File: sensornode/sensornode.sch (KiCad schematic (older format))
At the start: 24 parts, among them J1 Conn_01x02, J2 Conn_01x06_Male, J3 Conn_01x04_Male, J4 USB_B_Micro, Q1 MMBT3904, U1 ESP-12F, U2 MQ-135, U3 LTC4055, U4 MIC5504-3.3YM5

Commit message: update to latest
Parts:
- RV1: footprint Potentiometer_THT:Potentiometer_ACP_CA6-H2,5_Horizontal -> Potentiometer_THT:Potentiometer_Bourns_3266X_Horizontal
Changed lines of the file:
@@
 F 0 "RV1" V 7035 1550 50  0000 C CNN
 F 1 "100k" V 6944 1550 50  0000 C CNN
-F 2 "Potentiometer_THT:Potentiometer_ACP_CA6-H2,5_Horizontal" H 7150 1550 50  0001 C CNN
+F 2 "Potentiometer_THT:Potentiometer_Bourns_3266X_Horizontal" H 7150 1550 50  0001 C CNN
 F 3 "~" H 7150 1550 50  0001 C CNN
 	1    7150 1550

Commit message: add c6, relayout
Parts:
- added C6: 10u ceramic, Capacitor_SMD:C_0805_2012Metric, symbol Device:C
- added R10: 1k8, Resistor_SMD:R_0603_1608Metric, symbol Device:R
- U2: symbol Sensor_Gas:MQ-135 -> sensornode-rescue:MQ-135-Sensor_Gas
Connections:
- wire segments 101 -> 105
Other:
- moved on the sheet: RV1
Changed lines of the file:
@@
 $EndDescr
 $Comp
-L Sensor_Gas:MQ-135 U2
+L sensornode-rescue:MQ-135-Sensor_Gas U2
 U 1 1 5CC7BF70
 P 6100 1750
@@
 $EndComp
 Wire Wire Line
-	5550 1450 5150 1450
-Wire Wire Line
-	6600 1550 6750 1550
+	5550 1450 5300 1450
 Wire Wire Line
 	6600 2000 7000 2000
@@
 L power:GND #PWR016
 U 1 1 5CCBD0AA
-P 7550 1600
-F 0 "#PWR016" H 7550 1350 50  0001 C CNN
-F 1 "GND" H 7555 1427 50  0000 C CNN
-F 2 "" H 7550 1600 50  0001 C CNN
-F 3 "" H 7550 1600 50  0001 C CNN
-	1    7550 1600
+P 7750 1600
+F 0 "#PWR016" H 7750 1350 50  0001 C CNN
+F 1 "GND" H 7755 1427 50  0000 C CNN
+F 2 "" H 7750 1600 50  0001 C CNN
+F 3 "" H 7750 1600 50  0001 C CNN
+	1    7750 1600
 	1    0    0    -1
 $EndComp
@@
 L Device:R_POT RV1
 U 1 1 5CCBD83F
-P 7150 1550
-F 0 "RV1" V 7035 1550 50  0000 C CNN
-F 1 "100k" V 6944 1550 50  0000 C CNN
-F 2 "Potentiometer_THT:Potentiometer_Bourns_3266X_Horizontal" H 7150 1550 50  0001 C CNN
-F 3 "~" H 7150 1550 50  0001 C CNN
-	1    7150 1550
+P 7350 1550
+F 0 "RV1" V 7235 1550 50  0000 C CNN
+F 1 "100k" V 7144 1550 50  0000 C CNN
+F 2 "Potentiometer_THT:Potentiometer_Bourns_3266X_Horizontal" H 7350 1550 50  0001 C CNN
+F 3 "~" H 7350 1550 50  0001 C CNN
+	1    7350 1550
 	0    -1   -1   0
 $EndComp
 Wire Wire Line
-	7300 1550 7550 1550
-Wire Wire Line
-	7550 1550 7550 1600
-Wire Wire Line
-	7150 1400 7550 1400
-Wire Wire Line
-	7550 1400 7550 1550
-Connection ~ 7550 1550
-Wire Wire Line
-	6750 1550 6750 1150
-Connection ~ 6750 1550
-Wire Wire Line
-	6750 1550 7000 1550
-Text Label 6750 1300 0    50   ~ 0
+	7500 1550 7750 1550
+Wire Wire Line
+	7750 1550 7750 1600
+Wire Wire Line
+	7350 1400 7750 1400
+Wire Wire Line
+	7750 1400 7750 1550
+Connection ~ 7750 1550
+Text Label 7100 1300 0    50   ~ 0
 mq135_adc
 Wire Wire Line
@@
 Connection ~ 6150 4800
 Wire Wire Line
-	5150 2000 5550 2000
+	5150 2000 5300 2000
 $Comp
 L Connector:USB_B_Micro J4
@@
 	1    0    0    -1
 $EndComp
+$Comp
+L Device:C C6
+U 1 1 5CE46D1C
+P 5300 1850
+F 0 "C6" H 5415 1896 50  0000 L CNN
+F 1 "10u ceramic" H 5415 1805 50  0000 L CNN
+F 2 "Capacitor_SMD:C_0805_2012Metric" H 5338 1700 50  0001 C CNN
+F 3 "https://www.samsungsem.com/kr/support/product-search/mlcc/__icsFiles/afieldfile/2019/05/10/19-CL21A106KPFNNNE.pdf" H 5300 1850 50  0001 C CNN
+	1    5300 1850
+	1    0    0    -1
+$EndComp
+Connection ~ 5300 2000
+Wire Wire Line
+	5300 2000 5550 2000
+Wire Wire Line
+	5300 1700 5300 1450
+Connection ~ 5300 1450
+Wire Wire Line
+	5300 1450 5150 1450
+$Comp
+L Device:R R10
+U 1 1 5CE5CB49
+P 6850 1550
+F 0 "R10" V 6643 1550 50  0000 C CNN
+F 1 "1k8" V 6734 1550 50  0000 C CNN
+F 2 "Resistor_SMD:R_0603_1608Metric" V 6780 1550 50  0001 C CNN
+F 3 "~" H 6850 1550 50  0001 C CNN
+	1    6850 1550
+	0    1    1    0
+$EndComp
+Wire Wire Line
+	6600 1550 6700 1550
+Wire Wire Line
+	7000 1550 7100 1550
+Wire Wire Line
+	7100 1300 7100 1550
+Connection ~ 7100 1550
+Wire Wire Line
+	7100 1550 7200 1550
 $EndSCHEMATC

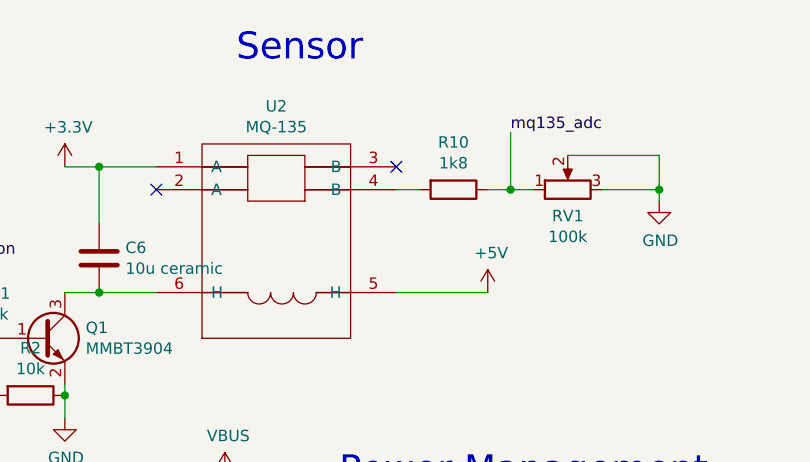
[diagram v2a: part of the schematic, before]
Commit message: tweaks, add jumper for programming
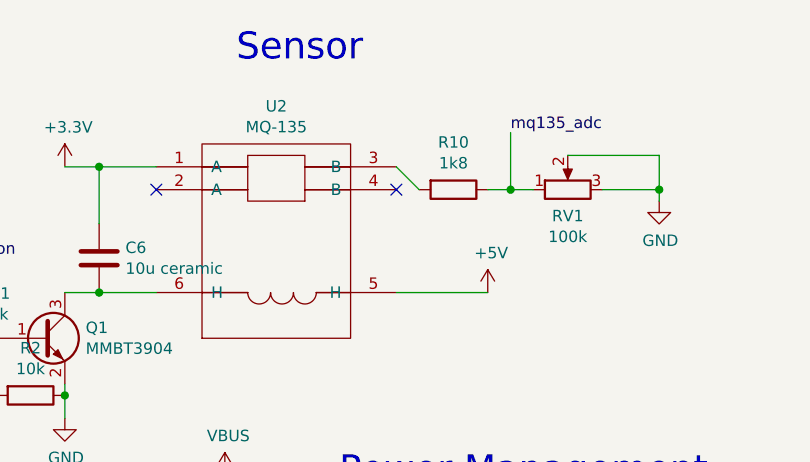
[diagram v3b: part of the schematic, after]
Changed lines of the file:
@@
 	7350 4050 7350 4450
 NoConn ~ 5550 1550
-NoConn ~ 6600 1450
 NoConn ~ 3500 2750
 NoConn ~ 3500 2850
@@
 $EndComp
 Wire Wire Line
-	6600 1550 6700 1550
-Wire Wire Line
 	7000 1550 7100 1550
 Wire Wire Line
@@
 Wire Wire Line
 	7100 1550 7200 1550
+Wire Wire Line
+	6600 1450 6700 1550
+NoConn ~ 6600 1550
 $EndSCHEMATC

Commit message: add missing libs and footprints, add jumper for programming
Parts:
- added JP1: SolderJumper_2_Open, Jumper:SolderJumper-2_P1.3mm_Open_Pad1.0x1.5mm, symbol Jumper:SolderJumper_2_Open
- U2: symbol sensornode-rescue:MQ-135-Sensor_Gas -> locals:MQ-135-Sensor_Gas
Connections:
- wire segments 105 -> 106
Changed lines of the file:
@@
 $EndDescr
 $Comp
-L sensornode-rescue:MQ-135-Sensor_Gas U2
+L locals:MQ-135-Sensor_Gas U2
 U 1 1 5CC7BF70
 P 6100 1750
@@
 Text Label 3650 2550 0    50   ~ 0
 RX
-Text Label 3600 3250 0    50   ~ 0
+Text Label 3850 3750 0    50   ~ 0
 ~RST
 $Comp
@@
 	6600 1450 6700 1550
 NoConn ~ 6600 1550
+$Comp
+L Jumper:SolderJumper_2_Open JP1
+U 1 1 5CEDCCCC
+P 3850 3400
+F 0 "JP1" V 3804 3468 50  0000 L CNN
+F 1 "SolderJumper_2_Open" V 3895 3468 50  0000 L CNN
+F 2 "Jumper:SolderJumper-2_P1.3mm_Open_Pad1.0x1.5mm" H 3850 3400 50  0001 C CNN
+F 3 "~" H 3850 3400 50  0001 C CNN
+	1    3850 3400
+	0    1    1    0
+$EndComp
+Wire Wire Line
+	3850 3550 3850 3750
 $EndSCHEMATC

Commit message: add acpower indication
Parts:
- J1: footprint Connector_JST:JST_EH_B02B-EH-A_1x02_P2.50mm_Vertical -> Connector_JST:JST_PH_B2B-PH-K_1x02_P2.00mm_Vertical
- R10: value 1k8 -> 6k8
- U2: symbol locals:MQ-135-Sensor_Gas -> sensornode-rescue:MQ-135-Sensor_Gas-locals
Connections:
- net labels added: ~acpr
- wire segments 106 -> 110
- no-connect marks 17 -> 15
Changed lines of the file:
@@
 $EndDescr
 $Comp
-L locals:MQ-135-Sensor_Gas U2
+L sensornode-rescue:MQ-135-Sensor_Gas-locals U2
 U 1 1 5CC7BF70
 P 6100 1750
@@
 F 0 "J1" H 8130 3442 50  0000 L CNN
 F 1 "Conn_01x02" H 8130 3351 50  0000 L CNN
-F 2 "Connector_JST:JST_EH_B02B-EH-A_1x02_P2.50mm_Vertical" H 8050 3450 50  0001 C CNN
+F 2 "Connector_JST:JST_PH_B2B-PH-K_1x02_P2.00mm_Vertical" H 8050 3450 50  0001 C CNN
 F 3 "~" H 8050 3450 50  0001 C CNN
 	1    8050 3450
 	1    0    0    -1
 $EndComp
-Wire Wire Line
-	7850 3550 7850 3900
-Wire Wire Line
-	7850 3450 6950 3450
 $Comp
 L power:GND #PWR015
 U 1 1 5CCC5953
-P 7850 3900
-F 0 "#PWR015" H 7850 3650 50  0001 C CNN
-F 1 "GND" H 7855 3727 50  0000 C CNN
-F 2 "" H 7850 3900 50  0001 C CNN
-F 3 "" H 7850 3900 50  0001 C CNN
-	1    7850 3900
-	1    0    0    -1
+P 7700 3450
+F 0 "#PWR015" H 7700 3200 50  0001 C CNN
+F 1 "GND" H 7705 3277 50  0000 C CNN
+F 2 "" H 7700 3450 50  0001 C CNN
+F 3 "" H 7700 3450 50  0001 C CNN
+	1    7700 3450
+	0    1    1    0
 $EndComp
 Wire Wire Line
@@
 	7350 4050 7350 4450
 NoConn ~ 5550 1550
-NoConn ~ 3500 2750
 NoConn ~ 3500 2850
 NoConn ~ 3500 2950
@@
 NoConn ~ 2300 2850
 NoConn ~ 6950 3550
-NoConn ~ 6150 3550
 NoConn ~ 6150 3650
 NoConn ~ 2650 6300
@@
 P 6850 1550
 F 0 "R10" V 6643 1550 50  0000 C CNN
-F 1 "1k8" V 6734 1550 50  0000 C CNN
+F 1 "6k8" V 6734 1550 50  0000 C CNN
 F 2 "Resistor_SMD:R_0603_1608Metric" V 6780 1550 50  0001 C CNN
 F 3 "~" H 6850 1550 50  0001 C CNN
@@
 Wire Wire Line
 	3850 3550 3850 3750
+Wire Wire Line
+	6950 3450 7550 3450
+Wire Wire Line
+	7550 3450 7550 3550
+Wire Wire Line
+	7550 3550 7850 3550
+Wire Wire Line
+	7700 3450 7850 3450
+Wire Wire Line
+	6150 3550 5850 3550
+Wire Wire Line
+	3500 2750 3900 2750
+Text Label 3700 2750 0    59   ~ 0
+~acpr
+Text Label 5900 3550 0    59   ~ 0
+~acpr
 $EndSCHEMATC
